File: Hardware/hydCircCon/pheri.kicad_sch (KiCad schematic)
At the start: 39 parts, among them J11 Conn_01x04, J12 Conn_01x02, J13 Conn_01x02, J14 Conn_01x03, J15 Conn_01x03, J3 Conn_01x03, J4 Conn_01x03, U5 TMP451, U6 DRV8231ADSGR, U7 DRV8231ADSGR

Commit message: wip
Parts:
- R27, R28: value 50R -> 51R
- R6, R7: value 1k -> 100R
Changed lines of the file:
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@@
       (effects (font (size 1.27 1.27)) (justify right))
     )
-    (property "Value" "1k" (id 1) (at 102.87 152.4 90)
+    (property "Value" "100R" (id 1) (at 104.14 152.4 90)
       (effects (font (size 1.27 1.27)) (justify right))
     )
@@
       (effects (font (size 1.27 1.27)) (justify right))
     )
-    (property "Value" "1k" (id 1) (at 102.87 142.24 90)
+    (property "Value" "100R" (id 1) (at 104.14 142.24 90)
       (effects (font (size 1.27 1.27)) (justify right))
     )
@@
       (effects (font (size 1.27 1.27)) (justify left))
     )
-    (property "Value" "50R" (id 1) (at 101.6 57.15 90)
+    (property "Value" "51R" (id 1) (at 101.6 57.15 90)
       (effects (font (size 1.27 1.27)) (justify left))
     )
@@
       (effects (font (size 1.27 1.27)) (justify left))
     )
-    (property "Value" "50R" (id 1) (at 101.6 49.53 90)
-      (effects (font (size 1.27 1.27)) (justify left))
-    )
+    (property "Value" "51R" (id 1) (at 101.6 49.53 90)
+      (effects (font (size 1.27 1.27)) (justify left))
+    )

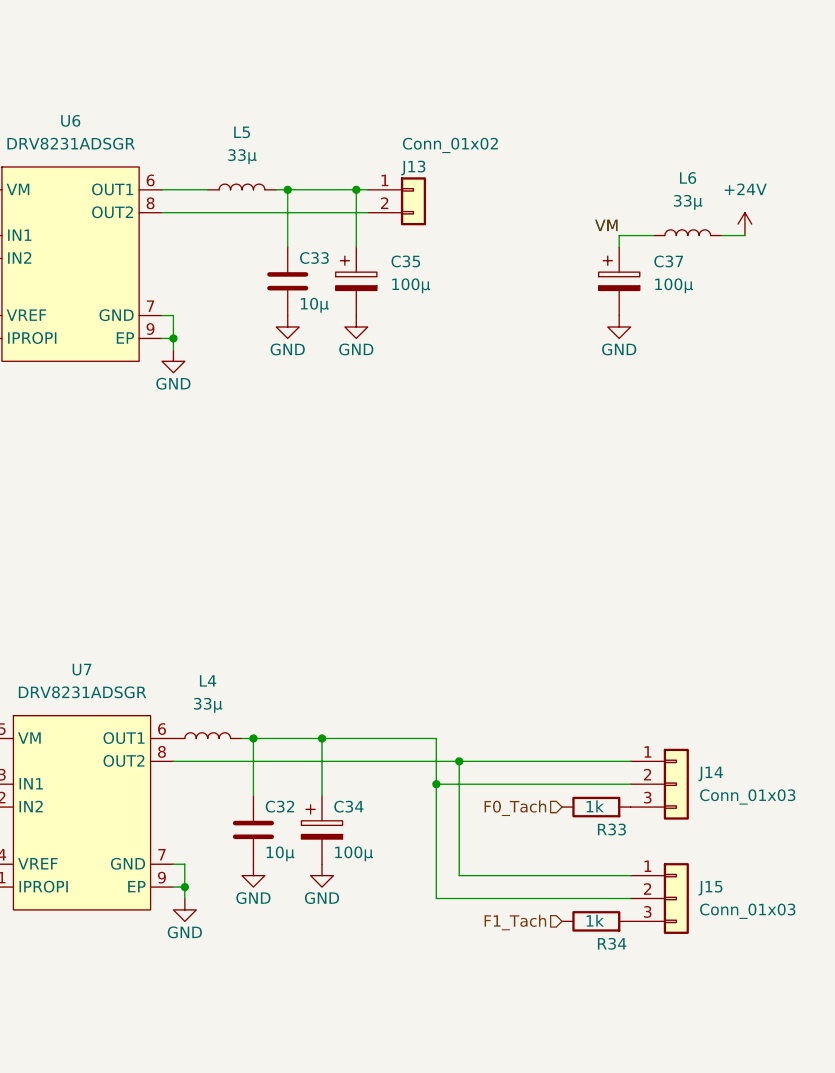
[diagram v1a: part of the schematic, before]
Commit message: modified motor output
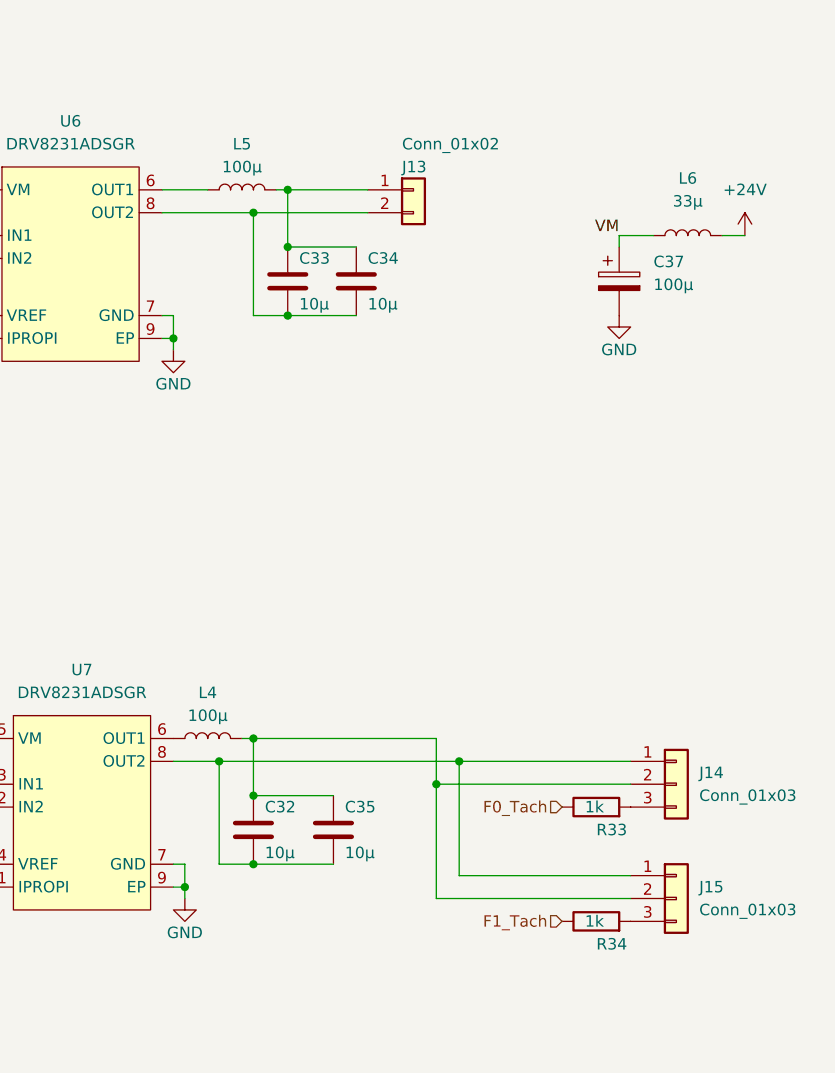
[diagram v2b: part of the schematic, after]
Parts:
- removed C34, C35: 100µ, Capacitor_THT:CP_Radial_D6.3mm_P2.50mm, symbol Device:C_Polarized
- added C34, C35: 10µ, Capacitor_SMD:C_1210_3225Metric, symbol Device:C
- L4, L5: value 33µ -> 100µ
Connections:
- net GND: no longer C32.1, C33.1
- net at C33.2, J13.1 (Pin_1), L5.2: now also C34.2
- net at J13.2 (Pin_2), U6.8 (OUT2): now also C33.1, C34.1
- net at C32.2, J14.2 (Pin_2), J15.2 (Pin_2)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: now also C35.2
- net at J14.1 (Pin_1), J15.1 (Pin_1), U7.8 (OUT2): now also C32.1, C35.1
